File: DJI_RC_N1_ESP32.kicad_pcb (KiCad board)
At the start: 2 copper layers, 57 x 73 mm, 57 parts, among them J4 WE 665102131822, J5 USB_C_Receptacle_USB2.0_16P, Q1 BSS84, Q2 BSS670S2, Q3 BSS670S2, Q4 BSS670S2, SW1 SW_DPST, SW2 SW_DPST, U16 USBLC6-2SC6, U2 ESP32-S3-WROOM-1U, U3 MIC5205-3.3YM5, U4 MCP73833-xxx-UN

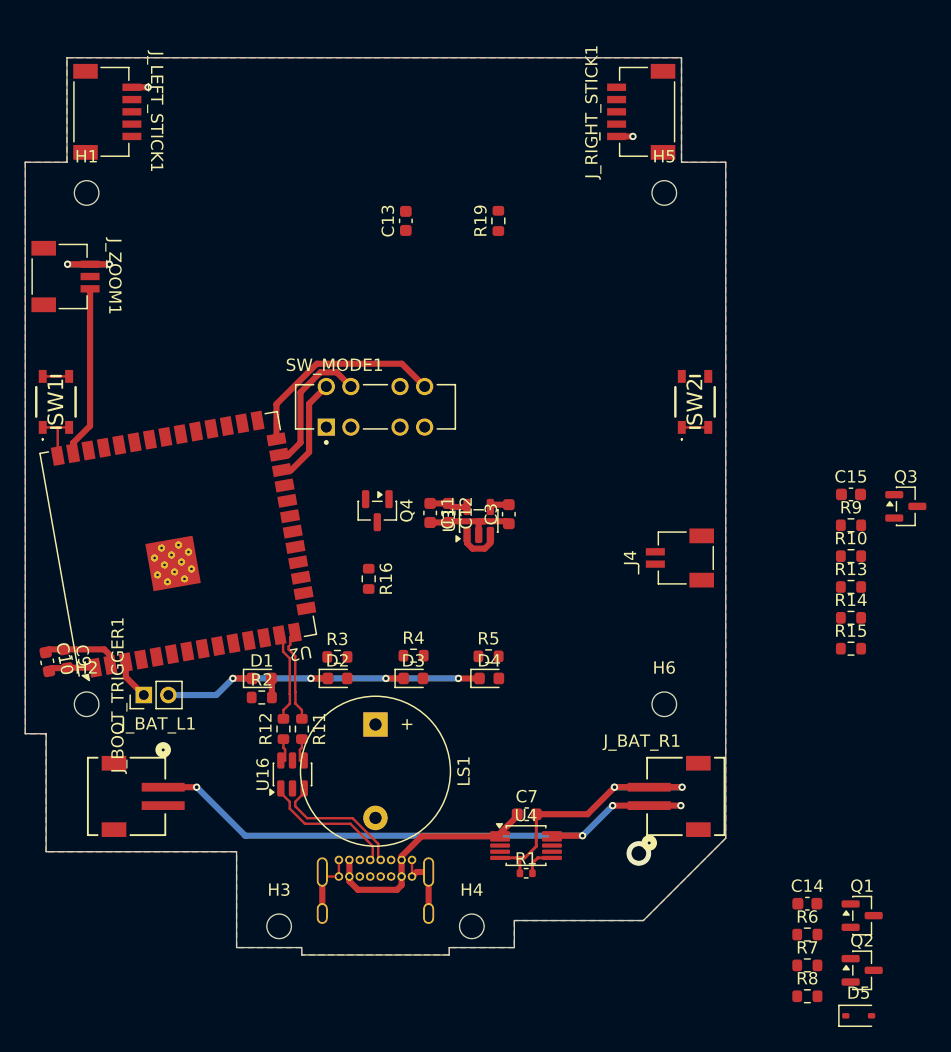
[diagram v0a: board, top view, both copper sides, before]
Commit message: Board had been routedy
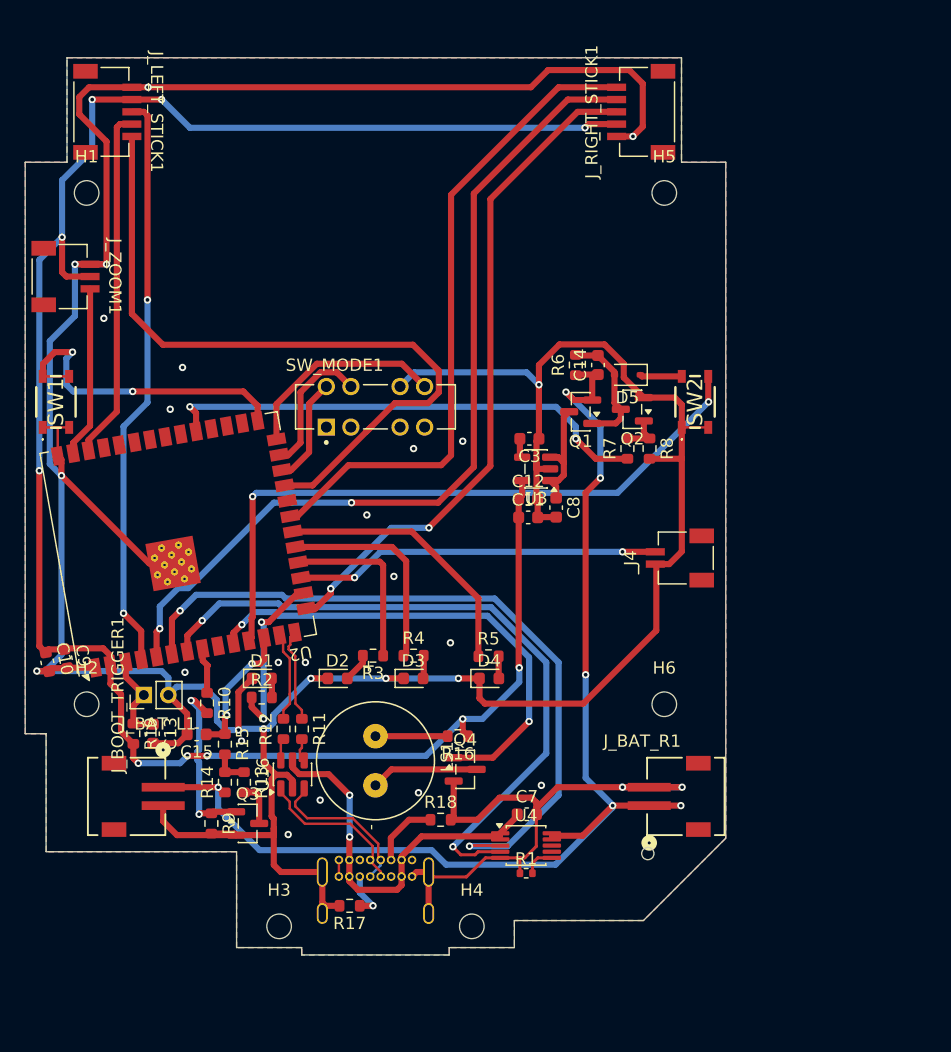
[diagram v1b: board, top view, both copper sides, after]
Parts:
- added C8: 4u7, Capacitor_SMD:C_0603_1608Metric, F.Cu at (43.2, 36.6)
- added R17: 5K1, Resistor_SMD:R_0603_1608Metric, F.Cu at (26.4, 69.0)
- added R18: 5K1, Resistor_SMD:R_0603_1608Metric, F.Cu at (33.8, 62.0)
- LS1: footprint Buzzer_Beeper:Buzzer_12x9.5RM7.6 -> footprints:XDCR_CMT-9605-85T
- moved Q3 59.4 mm to (18.1, 62.3)
- moved R9 57.4 mm to (15.2, 62.3), turned to -90 degrees
- moved C15 56.7 mm to (13.9, 55.0), turned to 180 degrees
- moved D5 55.4 mm to (49.0, 25.8), turned to 180 degrees
- moved R10 53.7 mm to (14.8, 52.5), turned to -90 degrees
- moved R14 52.7 mm to (16.2, 59.0), turned to 90 degrees
- moved R13 51.9 mm to (17.8, 59.0), turned to -90 degrees
- moved R15 51.5 mm to (16.2, 55.9), turned to -90 degrees
- moved R19 51.2 mm to (8.80, 55.0), turned to -90 degrees
- moved R6 50.0 mm to (44.8, 25.0), turned to 90 degrees
- moved Q2 49.3 mm to (49.4, 28.6), turned to 180 degrees
- moved C14 47.0 mm to (46.6, 25.0), turned to 90 degrees
- moved Q1 47.0 mm to (45.2, 28.8), turned to 180 degrees
- moved C13 46.5 mm to (10.4, 55.0), turned to -90 degrees
- moved R8 46.4 mm to (50.8, 31.8), turned to -90 degrees
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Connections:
- J5 pad A5: unconnected-(J5-CC1-PadA5) -> Net-(J5-CC1)
- J5 pad B5: unconnected-(J5-CC2-PadB5) -> Net-(J5-CC2)
- U2 pad 16: BTN_FN -> LED_1
- U2 pad 18: LED_4 -> LED_2
- U2 pad 20: LED_2 -> LED_4
- U2 pad 21: LED_1 -> BTN_CAM_CHANGE
- U2 pad 23: BTN_CAM_CHANGE -> BTN_FN
- U2 pad 4: AD3 -> AD0
- U2 pad 5: AD0 -> AD3
- U2 pad 8: unconnected-(U2-GPIO15/U0RTS/ADC2_CH4/XTAL_32K_P-Pad8) -> MEASURE_VBAT_EN
- U3 pad 1: VBAT -> VBAT_SWITCHED
- U3 pad 3: VBAT -> VBAT_SWITCHED
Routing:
- net GND: track 96.5 -> 362.5 mm, vias 10 -> 30
- net +3.3V: track 9.47 -> 163.2 mm, vias 0 -> 10
- net AD3: track 0.00 -> 71.5 mm, vias 0 -> 2
- net CHARGER_ST1: track 0.00 -> 59.7 mm, vias 0 -> 2
- net BTN_FN: track 0.00 -> 59.3 mm
- net CHARGER_ST2: track 0.00 -> 55.9 mm, vias 0 -> 2
- net AD2: track 0.00 -> 55.0 mm, vias 0 -> 2
- net BTN_PWR_MCU: track 0.00 -> 54.2 mm, vias 0 -> 2
- net BTN_CAM_CHANGE: track 0.00 -> 53.4 mm
- net AD0: track 0.00 -> 47.1 mm, vias 0 -> 2
- net VBAT: track 51.4 -> 97.6 mm, vias 4 -> 6
- net KEEP_PWR: track 0.00 -> 40.2 mm, vias 0 -> 2
- net BUZZER_PWM: track 0.00 -> 39.7 mm, vias 0 -> 2
- net BTN_SHOOT: track 0.00 -> 29.7 mm, vias 0 -> 2
- net AD1: track 0.00 -> 28.6 mm
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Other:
- outline, holes or cut-outs redrawn
- copper layers 2 -> 4
